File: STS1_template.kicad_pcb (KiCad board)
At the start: 4 copper layers, 85 x 85 mm, 152 parts, among them IC1 STM32F411RET6TR, IC2 STWD100PYW83F, J1 Conn_01x01_Male, J10 Conn_01x01_Male, J11 Conn_01x01_Male, J12 Conn_01x01_Male, J13 Conn_01x01_Male, J14 Conn_01x01_Male, J15 Conn_01x01_Male, J16 Conn_01x01_Male, J17 Conn_01x01_Male, J18 Conn_01x01_Male, J19 Conn_01x01_Male, J2 Conn_01x05_Female, J20 Conn_01x01_Male, J21 Conn_01x01_Male, J22 Conn_01x01_Male, J23 Conn_01x01_Male, J24 Conn_01x01_Male, J25 Conn_01x01_Male, J26 Conn_01x01_Male, J27 Conn_01x01_Male, J28 Conn_01x01_Male, J29 Conn_01x01_Male, J3 Conn_01x01_Male, J30 Conn_01x01_Male, J31 Conn_01x01_Male, J32 Conn_01x01_Male, J33 Conn_01x01_Male, J34 Conn_01x01_Male, J35 Conn_01x01_Male, J36 Conn_01x01_Male, J37 Conn_01x01_Male, J38 Conn_01x01_Male, J39 Conn_Coaxial, J4 Conn_01x01_Male, J40 Conn_Coaxial, J41 Conn_01x01_Male, J42 Conn_01x01_Male, J43 Conn_01x01_Male, J44 Conn_01x01_Male, J45 Conn_01x01_Male, J46 Conn_01x01_Male, J47 Conn_01x01_Male, J48 Conn_01x01_Male, J49 Conn_01x01_Male, J5 Conn_01x01_Male, J50 Conn_01x01_Male, J51 Conn_01x01_Male, J52 Conn_01x01_Male, J53 Conn_01x01_Male, J54 Conn_01x01_Male, J55 Conn_01x01_Female, J56 Conn_01x01_Male, J57 Conn_01x01_Male, J58 Conn_01x01_Male, J59 Conn_01x01_Male, J6 Conn_01x01_Male, J60 Conn_01x01_Male, J61 Conn_01x01_Male, J62 Conn_01x01_Male, J63 Conn_01x01_Male, J64 Conn_01x02_Male, J65 Conn_01x02_Male, J66 Conn_01x02_Male, J67 Conn_01x02_Male, J68 Conn_01x02_Male, J69 Conn_01x02_Male, J7 Conn_01x01_Male, J70 Conn_01x02_Male, J71 Conn_01x02_Male, J8 Conn_01x01_Male, J9 Conn_01x01_Male, U1 coordinate_system, U2 TPS61288, Y1 12MHz

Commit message: final version1
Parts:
- removed J1, J13, J14, J15, J16, J17, J18, J19, J20, J21, J22, J23, J24, J25, J26, J27, J28, J29, J32, J33, J34, J35, J36, J37, J38, J42, J43, J47, J48, J49, J56, J57, J58, J59, J60, J61, J62, J63, J9: Conn_01x01_Male, Connector_PinHeader_2.54mm:PinHeader_1x01_P2.54mm_Vertical
- removed the J3 at (255.5, 89.4)
- removed the J3 at (238.0, 134.1)
- removed the J4 at (250.8, 94.1)
- removed the J4 at (242.6, 134.1)
- removed J64, J65, J66, J67, J68, J69, J70, J71: Conn_01x02_Male, Connector_PinHeader_2.54mm:PinHeader_1x02_P2.54mm_Vertical
- removed JP1, JP2, JP3, JP4, JP5, JP6, JP7, JP8: Jumper_NC_Dual, Connector_PinHeader_2.54mm:PinHeader_1x02_P2.54mm_Vertical
- added C33: 4.7µF, Capacitor_SMD:C_0805_2012Metric, F.Cu at (131.8, 61.0)
- added C34: 0.1µ, Capacitor_SMD:C_0805_2012Metric, F.Cu at (140.8, 66.6)
- added C35: 4.7µF, Capacitor_SMD:C_0805_2012Metric, F.Cu at (137.6, 61.0)
- added D4: LED, LED_SMD:LED_0805_2012Metric, F.Cu at (133.9, 67.2)
- added J3: Conn_ARM_JTAG_SWD_10, Connector_PinHeader_1.27mm:PinHeader_2x05_P1.27mm_Vertical_SMD, F.Cu at (167.4, 121.7)
- added J4: Conn_01x01_Male, Connector_PinHeader_2.54mm:PinHeader_1x01_P2.54mm_Vertical, F.Cu at (272.1, 85.5)
- added R9: 1k, Resistor_SMD:R_0805_2012Metric, F.Cu at (137.8, 67.2)
- added U3: MCP1725-3302E_MC, STS1_3V3:MCP1725-3302E&slash_MC, F.Cu at (134.9, 64.5)
- C28, C29, C30, C31: moved to F.Cu
- J10, J11, J12, J6, J7, J8: value Conn_01x01_Male -> Conn_01x03_Male; footprint Connector_PinHeader_2.54mm:PinHeader_1x01_P2.54mm_Vertical -> STS1library:PinHeader_1x03_P2.54mm_Vertical_umdieEcke
- J2: value Conn_01x05_Female -> Conn_01x03_Male; footprint Connector_PinHeader_2.54mm:PinHeader_1x05_P2.54mm_Horizontal -> STS1library:PinHeader_1x03_P2.54mm_Vertical_umdieEcke
- moved J12 107.8 mm to (154.3, 119.0), turned to 180 degrees
- moved J7 102.7 mm to (143.0, 52.5), turned to 180 degrees
- moved J8 76.0 mm to (162.2, 76.2), turned to 180 degrees
- moved J31 72.0 mm to (280.0, 105.2)
- moved J44 71.2 mm to (280.4, 92.5)
- moved J5 65.5 mm to (186.2, 110.5)
- moved J11 61.7 mm to (190.3, 106.0)
- moved J30 61.0 mm to (280.4, 85.2)
- moved J10 57.3 mm to (190.3, 113.5)
- moved J6 47.6 mm to (195.2, 80.5), turned to 270 degrees
- moved C29 42.0 mm to (136.6, 73.5), turned to 90 degrees
- moved C28 42.0 mm to (142.7, 73.5), turned to 90 degrees
- moved C30 42.0 mm to (130.6, 73.5), turned to 90 degrees
- moved C31 42.0 mm to (124.5, 73.5), turned to 90 degrees
- moved J41 38.7 mm to (280.3, 98.8)
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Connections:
- net /STS1_COBC_uC/PB3 renamed /STS1_COBC_uC/SWO
- net /STS1_COBC_uC/STM32_PA9(Watchdog_toggle) renamed /STS1_COBC_uC/WDT_Clear
- net /STS1_connector/EDU_SPI_1 renamed /STS1_Connector/EDU_SPI_1
- net /STS1_connector/EDU_SPI_2 renamed /STS1_Connector/EDU_SPI_2
- net /STS1_connector/EDU_SPI_3 renamed /STS1_Connector/EDU_SPI_3
- net /STS1_connector/EDU_SPI_4 renamed /STS1_Connector/EDU_SPI_4
- net /STS1_connector/EDU_SPI_5 renamed /STS1_Connector/EDU_SPI_5
- net /STS1_connector/EDU_SPI_6 renamed /STS1_Connector/EDU_SPI_6
- C21 pad 1: /STS1_PowerRegulation/VIN -> VBUS
- C22 pad 1: /STS1_PowerRegulation/VIN -> VBUS
- C23 pad 1: /STS1_PowerRegulation/VIN -> VBUS
- CSBI_1 pad 13: /STS1_connector/EDU_Heartbeat -> /EDU_Heartbeat
- CSBI_1 pad 14: /STS1_connector/EDU_Heartbeat -> /EDU_Heartbeat
- CSBI_1 pad 15: /STS1_connector/UART_COBC_EDU_1 -> /UART_COBC_EDU_1
- CSBI_1 pad 16: /STS1_connector/UART_COBC_EDU_1 -> /UART_COBC_EDU_1
- CSBI_1 pad 17: /STS1_connector/UART_COBC_EDU_2 -> /UART_COBC_EDU_2
- CSBI_1 pad 18: /STS1_connector/UART_COBC_EDU_2 -> /UART_COBC_EDU_2
- CSBI_1 pad 21: /STS1_connector/EDU_EN -> /EDU_EN
- CSBI_1 pad 22: /STS1_connector/EDU_EN -> /EDU_EN
- CSBI_1 pad 23: /STS1_connector/EDU_UPDATE -> /EDU_UPDATE
- CSBI_1 pad 24: /STS1_connector/EDU_UPDATE -> /EDU_UPDATE
- CSBI_2 pad 13: /STS1_connector/UCI_COBC_UART_1 -> /UCI_COBC_UART_1
- CSBI_2 pad 14: /STS1_connector/UCI_COBC_UART_1 -> /UCI_COBC_UART_1
- CSBI_2 pad 15: /STS1_connector/UCI_COBC_UART_2 -> /UCI_COBC_UART_2
- CSBI_2 pad 16: /STS1_connector/UCI_COBC_UART_2 -> /UCI_COBC_UART_2
- CSBI_2 pad 17: /STS1_connector/UCI_COBC_3V3 -> +3V3
- CSBI_2 pad 18: /STS1_connector/UCI_COBC_3V3 -> +3V3
- CSBI_2 pad 21: /STS1_connector/EPS_BAT_GOOD -> /EPS_BAT_GOOD
- CSBI_2 pad 22: /STS1_connector/EPS_BAT_GOOD -> /EPS_BAT_GOOD
- CSBI_2 pad 23: /STS1_connector/EPS_ANT_DEPLOYED -> /EPS_ANT_DEP
- CSBI_2 pad 24: /STS1_connector/EPS_ANT_DEPLOYED -> /EPS_ANT_DEP
- CSBI_2 pad 25: /STS1_connector/EPS_CHARGING -> /EPS_CHARGING
- CSBI_2 pad 26: /STS1_connector/EPS_CHARGING -> /EPS_CHARGING
- CSBI_2 pad 29: /STS1_connector/COBC_SPI_1 -> /COBC_SPI_1
- CSBI_2 pad 30: /STS1_connector/COBC_SPI_1 -> /COBC_SPI_1
- CSBI_2 pad 31: /STS1_connector/COBC_SPI_2 -> /COBC_SPI_2
- CSBI_2 pad 32: /STS1_connector/COBC_SPI_2 -> /COBC_SPI_2
- CSBI_2 pad 33: /STS1_connector/COBC_SPI_3 -> /COBC_SPI_3
- CSBI_2 pad 34: /STS1_connector/COBC_SPI_3 -> /COBC_SPI_3
- CSBI_2 pad 35: /STS1_connector/COBC_SPI_4 -> /COBC_SPI_4
- CSBI_2 pad 36: /STS1_connector/COBC_SPI_4 -> /COBC_SPI_4
- CSBI_2 pad 37: /STS1_connector/COBC_SPI_5 -> /COBC_SPI_5
- CSBI_2 pad 38: /STS1_connector/COBC_SPI_5 -> /COBC_SPI_5
- CSBI_2 pad 39: /STS1_connector/COBC_SPI_6 -> /COBC_SPI_6
- CSBI_2 pad 40: /STS1_connector/COBC_SPI_6 -> /COBC_SPI_6
- IC1 pad 15: /STS1_RF/RF4463_SDI -> /STS1_RF/LoRa_MOSI
- IC1 pad 16: Net-(IC1-Pad16) -> /UCI_COBC_UART_1
- IC1 pad 17: Net-(IC1-Pad17) -> /UCI_COBC_UART_2
- IC1 pad 2: /STS1_COBC_uC/PC13 -> /EPS_ANT_DEP
- IC1 pad 20: /STS1_RF/LoRa_NSS -> Net-(IC1-Pad20)
- IC1 pad 25: Net-(IC1-Pad25) -> /EDU_Heartbeat
- IC1 pad 26: Net-(IC1-Pad26) -> /EDU_EN
- IC1 pad 27: Net-(IC1-Pad27) -> /EDU_UPDATE
- IC1 pad 3: /STS1_COBC_uC/PC14 -> /EPS_CHARGING
- IC1 pad 33: /STS1_RF/RF4463_nSEL -> /STS1_COBC_uC/SPI4_NSS
- IC1 pad 34: /STS1_RF/RF4463_SPI_CLK -> /STS1_RF/LoRa_SPI_CLK
- IC1 pad 35: Net-(IC1-Pad35) -> /RF4463F30_SDN
- IC1 pad 36: Net-(IC1-Pad36) -> /LoRa_NRESET
- IC1 pad 37: Net-(IC1-Pad37) -> /RF4463F30_GPIO0
- IC1 pad 39: Net-(IC1-Pad39) -> /RF4463F30_GPIO1
- IC1 pad 4: /STS1_COBC_uC/PC15 -> /EPS_BAT_GOOD
- IC1 pad 40: Net-(IC1-Pad40) -> /STS1_RF/LoRa_NSS
- IC1 pad 41: Net-(IC1-Pad41) -> /STS1_RF/RF4463_nSEL
- IC1 pad 43: Net-(IC1-Pad43) -> /UART_COBC_EDU_2
- IC1 pad 44: /STS1_RF/RF4463_SDO -> /STS1_RF/LoRa_MISO
- IC1 pad 46: Net-(IC1-Pad46) -> /STS1_COBC_uC/SWDIO
- IC1 pad 49: Net-(IC1-Pad49) -> /STS1_COBC_uC/SWDCLK
- IC1 pad 50: /STS1_COBC_uC/PA15 -> /UART_COBC_EDU_1
- IC1 pad 51: /STS1_RF/LoRa_SPI_CLK -> /COBC_SPI_1
- IC1 pad 52: /STS1_RF/LoRa_MISO -> /COBC_SPI_3
- IC1 pad 53: /STS1_RF/LoRa_MOSI -> /COBC_SPI_2
- IC1 pad 54: /STS1_COBC_uC/PD2 -> /COBC_SPI_4
- IC1 pad 56: /STS1_COBC_uC/PB4 -> /COBC_SPI_5
- IC1 pad 57: /STS1_COBC_uC/PB5 -> /COBC_SPI_6
- IC2 pad 3: GND -> Net-(IC2-Pad3)
- J10 pad 1: /STS1_COBC_Memories/Flash_DataOutput -> GND
- J11 pad 1: /STS1_COBC_Memories/FRAM_CS -> GND
- J12 pad 1: /STS1_COBC_Memories/Flash_DataInput -> +3V3
- J2 pad 1: +3V3 -> GND
- J2 pad 2: Net-(IC1-Pad49) -> Net-(FLASH1-Pad7)
- J2 pad 3: GND -> +3V3
- J5 pad 1: /STS1_RF/RF4463_nSEL -> /STS1_COBC_uC/SPI4_NSS
- J6 pad 1: /STS1_COBC_Memories/FRAM_DataInput -> +3V3
- J7 pad 1: +3V3 -> GND
- J8 pad 1: +3V3 -> GND
- L1 pad 1: /STS1_PowerRegulation/VIN -> VBUS
- R2 pad 2: Net-(IC1-Pad49) -> /STS1_COBC_uC/SWDCLK
- R3 pad 2: Net-(IC1-Pad46) -> /STS1_COBC_uC/SWDIO
- RF1 pad 12: GND -> Net-(RF1-Pad12)
- RF1 pad 13: Net-(J66-Pad2) -> Net-(J7-Pad2)
- RF1 pad 14: Net-(J67-Pad2) -> Net-(J8-Pad2)
- RF1 pad 3: GND -> Net-(RF1-Pad3)
- RF1 pad 4: GND -> Net-(RF1-Pad4)
- RF1 pad 5: Net-(J65-Pad1) -> /LoRa_NRESET
- RF2 pad 10: /STS1_RF/RF4463_SDI -> /STS1_RF/LoRa_MOSI
- RF2 pad 11: /STS1_RF/RF4463_SDO -> /STS1_RF/LoRa_MISO
- RF2 pad 12: Net-(J70-Pad2) -> Net-(J11-Pad2)
- RF2 pad 13: Net-(J69-Pad2) -> Net-(J10-Pad2)
- RF2 pad 14: GND -> Net-(RF2-Pad14)
- RF2 pad 3: GND -> Net-(RF2-Pad3)
- RF2 pad 4: GND -> Net-(RF2-Pad4)
- RF2 pad 5: Net-(J68-Pad1) -> /RF4463F30_SDN
- RF2 pad 9: /STS1_RF/RF4463_SPI_CLK -> /STS1_RF/LoRa_SPI_CLK
- U2 pad 7: /STS1_PowerRegulation/VIN -> VBUS
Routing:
- net +3V3: track 56.2 -> 329.4 mm, vias 2 -> 15
- net /STS1_RF/RF4463_nSEL: track 0.00 -> 129.0 mm, vias 0 -> 3
- net /EDU_Heartbeat: track 0.00 -> 128.8 mm, vias 0 -> 3
- net /UART_COBC_EDU_2: track 0.00 -> 115.2 mm, vias 0 -> 5
- net /RF4463F30_SDN: track 0.00 -> 115.1 mm, vias 0 -> 1
- net /EDU_EN: track 0.00 -> 112.9 mm, vias 0 -> 7
- net +5V: track 84.0 -> 196.4 mm, vias 3 -> 7
- net Net-(J10-Pad2): track 0.00 -> 106.5 mm, vias 0 -> 2
- net /EDU_UPDATE: track 0.00 -> 104.4 mm, vias 0 -> 4
- net /STS1_RF/LoRa_SPI_CLK: track 0.00 -> 102.7 mm, vias 0 -> 5
- net /UCI_COBC_UART_1: track 0.00 -> 99.2 mm, vias 0 -> 4
- net /UART_COBC_EDU_1: track 0.00 -> 95.5 mm, vias 0 -> 3
- net /STS1_RF/LoRa_MISO: track 0.00 -> 86.3 mm, vias 0 -> 5
- net /STS1_COBC_uC/STM32_NRST: track 3.76 -> 87.5 mm, vias 0 -> 3
- net /STS1_RF/LoRa_MOSI: track 0.00 -> 83.7 mm, vias 0 -> 3
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
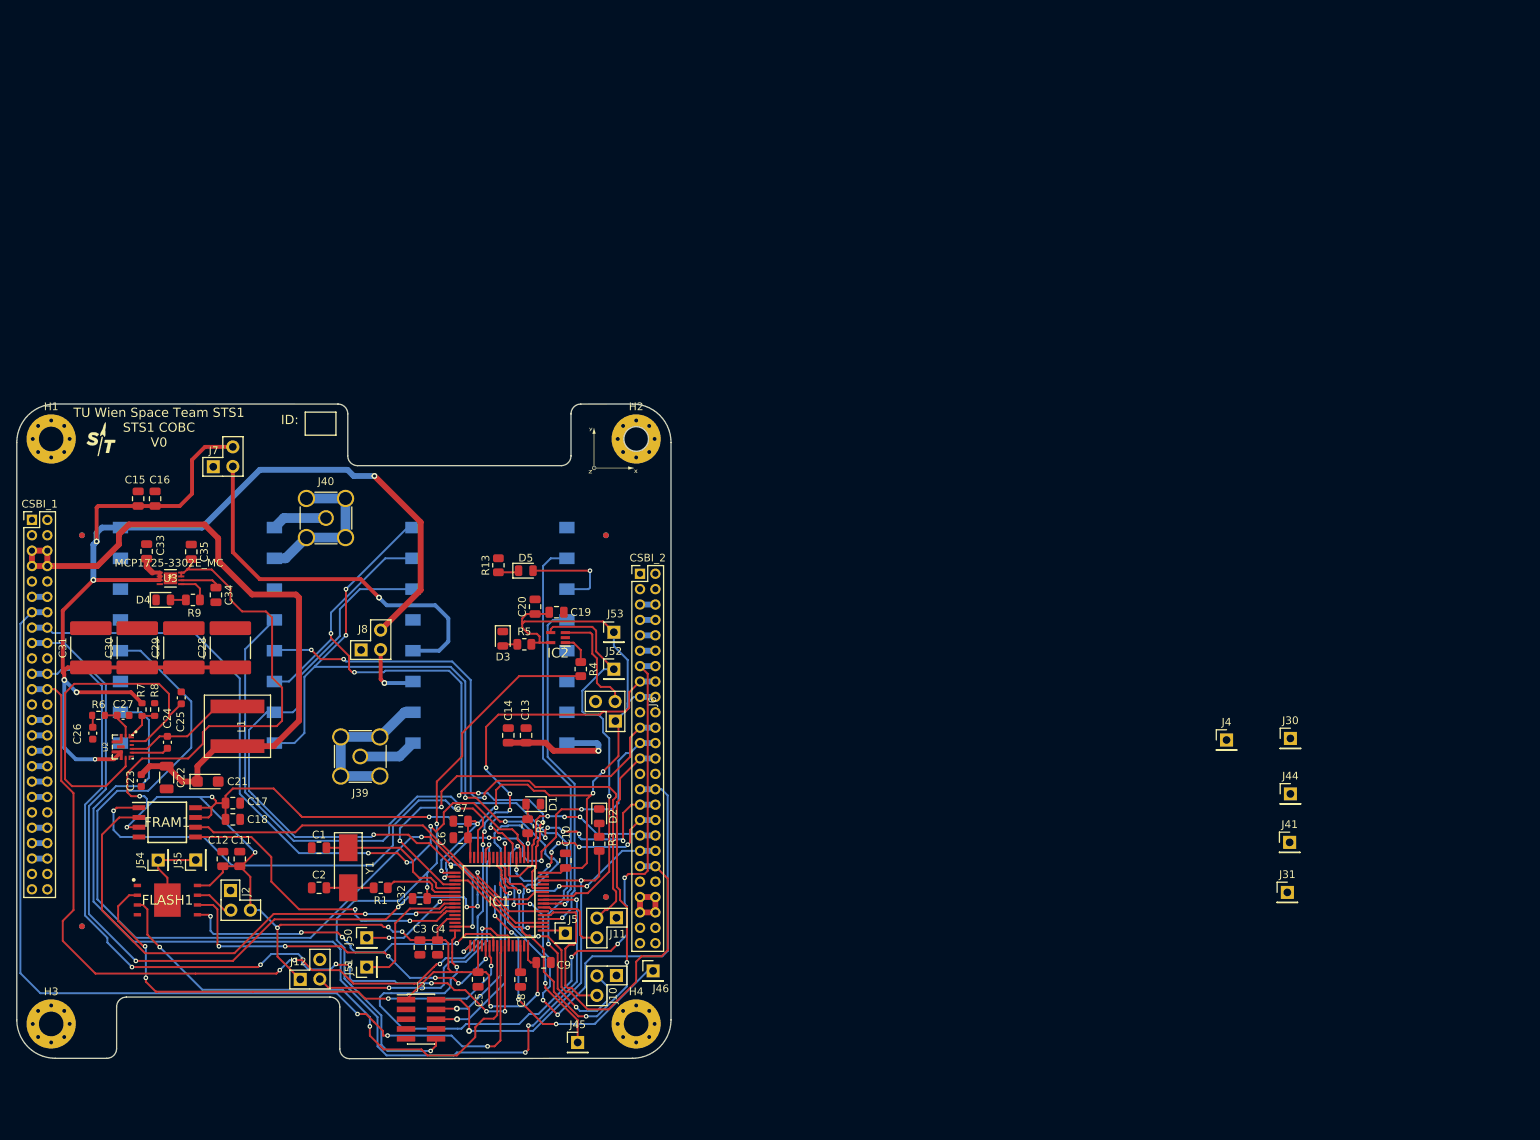
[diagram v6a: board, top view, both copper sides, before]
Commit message: added powerplane + testpoints + some debugging
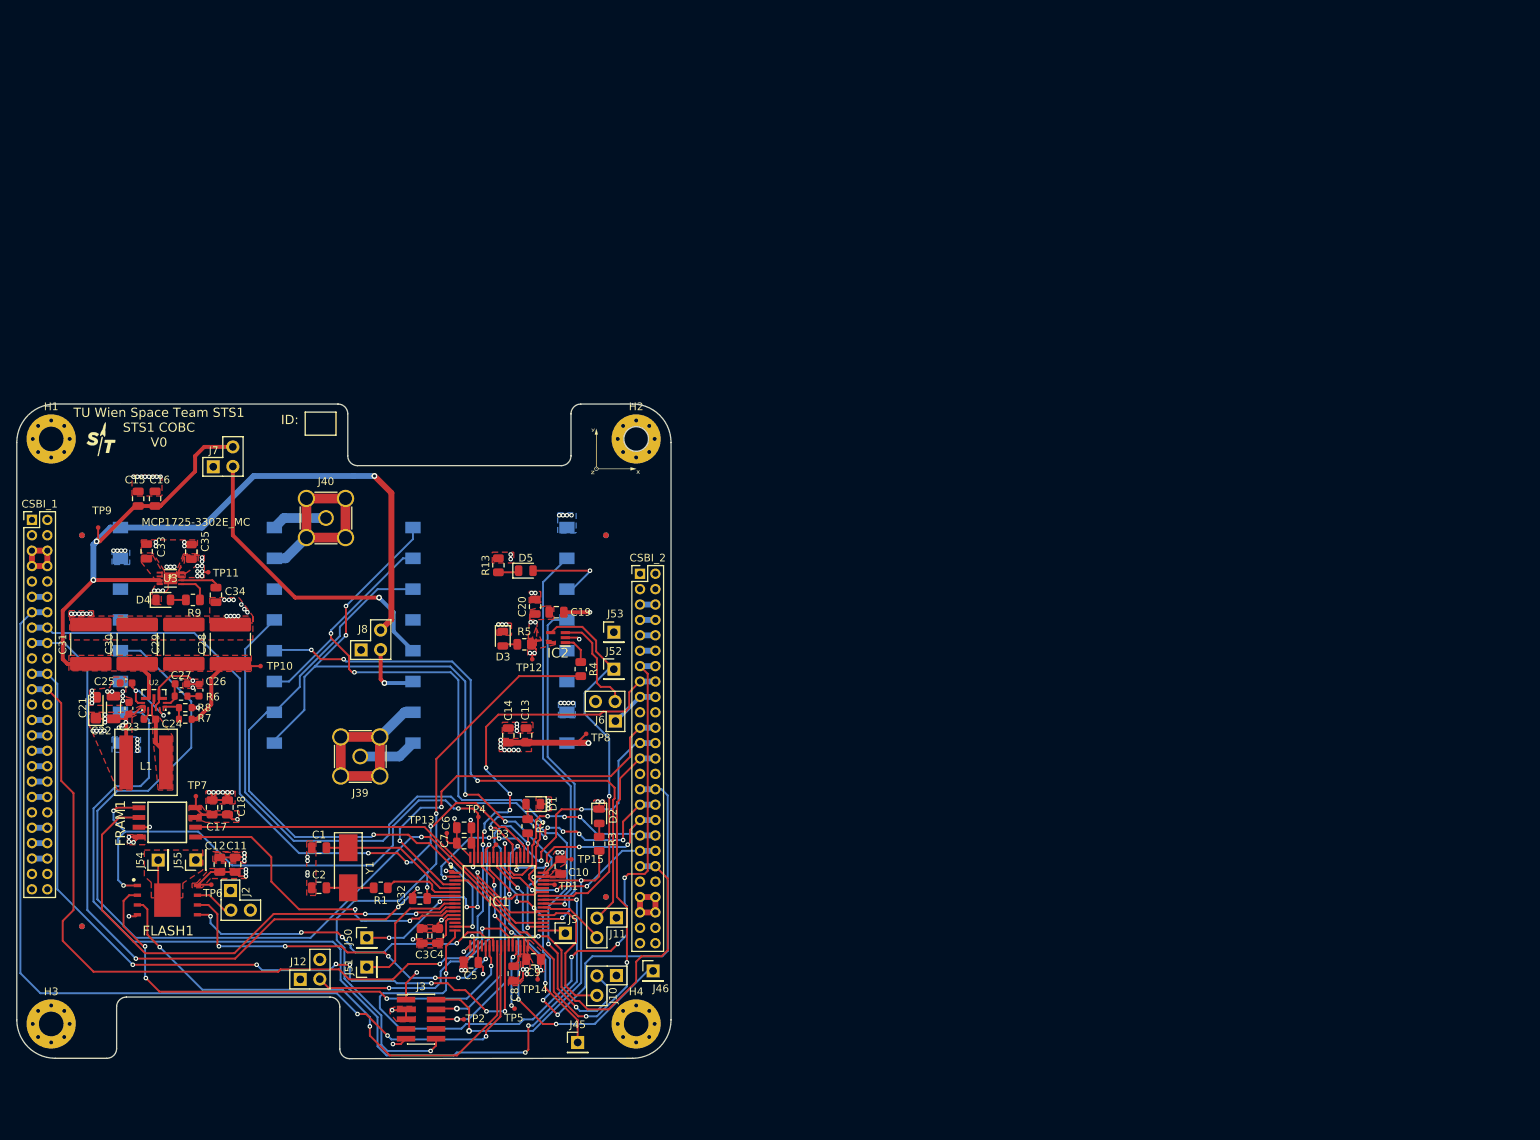
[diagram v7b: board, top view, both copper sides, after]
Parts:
- removed J30, J31, J4, J41, J44: Conn_01x01_Male, Connector_PinHeader_2.54mm:PinHeader_1x01_P2.54mm_Vertical
- added TP1: TestPoint, STS1library:STS1_Testpoint, F.Cu at (184.8, 104.2)
- added TP10: TestPoint, STS1library:STS1_Testpoint, F.Cu at (146.6, 75.8)
- added TP11: TestPoint, STS1library:STS1_Testpoint, F.Cu at (139.8, 63.6)
- added TP12: TestPoint, STS1library:STS1_Testpoint, F.Cu at (181.9, 75.0)
- added TP13: TestPoint, STS1library:STS1_Testpoint, F.Cu at (170.8, 97.5)
- added TP14: TestPoint, STS1library:STS1_Testpoint, F.Cu at (182.6, 116.5)
- added TP15: TestPoint, STS1library:STS1_Testpoint, F.Cu at (187.0, 101.0)
- added TP2: TestPoint, STS1library:STS1_Testpoint, F.Cu at (173.0, 121.8)
- added TP3: TestPoint, STS1library:STS1_Testpoint, F.Cu at (177.2, 99.0)
- added TP4: TestPoint, STS1library:STS1_Testpoint, F.Cu at (174.9, 95.5)
- added TP5: TestPoint, STS1library:STS1_Testpoint, F.Cu at (179.6, 120.3)
- added TP6: TestPoint, STS1library:STS1_Testpoint, F.Cu at (140.2, 104.2)
- added TP7: TestPoint, STS1library:STS1_Testpoint, F.Cu at (138.2, 92.8)
- added TP8: TestPoint, STS1library:STS1_Testpoint, F.Cu at (188.9, 84.7)
- added TP9: TestPoint, STS1library:STS1_Testpoint, F.Cu at (125.5, 57.9)
- moved C21 17.4 mm to (125.2, 81.2), turned to 90 degrees
- moved C26 14.9 mm to (138.6, 79.0), turned to 90 degrees
- moved L1 12.8 mm to (131.7, 88.3), turned to 0 degrees
- moved C22 11.4 mm to (127.5, 81.2), turned to 90 degrees
- moved R6 11.0 mm to (136.2, 79.8), turned to 0 degrees
- moved C23 9.54 mm to (129.5, 81.3), turned to 90 degrees
- moved C27 8.57 mm to (136.2, 78.2)
- moved C25 7.43 mm to (129.1, 78.0), turned to 180 degrees
- moved U2 7.32 mm to (132.7, 80.2), turned to 180 degrees
- moved R7 5.76 mm to (136.8, 82.8), turned to 180 degrees
- moved R8 3.99 mm to (136.8, 81.2), turned to 0 degrees
- moved C24 3.77 mm to (132.2, 82.8), turned to 0 degrees
- moved C7 2.89 mm to (173.0, 98.8), turned to 180 degrees
- moved C17 2.76 mm to (140.3, 94.2), turned to 270 degrees
- moved C5 2.39 mm to (173.9, 114.3), turned to 0 degrees
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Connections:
- net /STS1_RF/RF4463_nIRQ renamed Net-(RF2-Pad6)
- FLASH1 pad 1: /STS1_COBC_Memories/Flash_CS -> /STS1_COBC_Memories/FRAM_CS
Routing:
- net +3V3: track 329.4 -> 66.6 mm, vias 15 -> 26
- net GND: track 0.00 -> 78.8 mm, vias 0 -> 105
- net VBUS: track 99.6 -> 30.1 mm, vias 0 -> 10
- net +5V: track 196.4 -> 150.5 mm, vias 7 -> 11
- net Net-(C25-Pad1): track 47.8 -> 9.50 mm, vias 0 -> 2
- net Net-(J7-Pad2): track 50.8 -> 40.0 mm
- net Net-(IC1-Pad29): track 0.00 -> 8.60 mm, vias 0 -> 2
- net /STS1_COBC_Memories/FRAM_CS: track 67.1 -> 75.3 mm, vias 2 -> 3
- net /EDU_EN: track 112.9 -> 105.5 mm
- net Net-(C24-Pad2): track 16.0 -> 9.20 mm
- net /STS1_RF/RF4463_ANT_GND: track 20.5 -> 25.6 mm
- net /STS1_RF/LoRa_SMA_GND: track 20.9 -> 25.9 mm
- net Net-(FLASH1-Pad9): track 10.6 -> 5.71 mm
- net /STS1_RF/LoRa_SPI_CLK: track 102.7 -> 97.9 mm
- net /STS1_COBC_uC/PB9: track 37.9 -> 42.3 mm, vias 4 -> 5
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- added copper zone on F.Cu, net +3V3
- added copper zone on In2.Cu, net +3V3
- added copper zone on F.Cu, net +5V
- added copper zone on In2.Cu, net +5V
- added copper zone on B.Cu, net GND
- added copper zone on F.Cu, net GND
- added copper zone on F.Cu, net Net-(C24-Pad2)
- added copper zone on F.Cu, net Net-(FLASH1-Pad9)
- added copper zone on F.Cu, net VBUS
- added copper zone on In2.Cu, net VBUS

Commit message: finished prototype
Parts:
- VCC RF: renamed from TP8
- renumbered TP9 to 5V, TP10 to 5V, TP4 to FRAMCS, TP1 to PA12, TP5 to PB10, TP3 to PB6, TP2 to SWO, TP6 to VCC, TP7 to VCC, TP11 to VCC, TP12 to VCC, TP13 to VCC, TP14 to VCC, TP15 to VCC
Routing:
- net +3V3: track 66.6 -> 79.3 mm
